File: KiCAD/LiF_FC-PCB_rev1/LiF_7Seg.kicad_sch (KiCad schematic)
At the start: 9 parts, among them J33 DISP 5V0_{EN}, U13 74HCT595PW,118, U14 DC56-11EWA, U15 74HCT595PW,118

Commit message: fixing ERC bugs on schematic. Only MCU left
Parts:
- added TP29: DATA, TestPoint:TestPoint_Bridge_Pitch2.54mm_Drill1.0mm, symbol Connector:TestPoint
- added TP30: CLK, TestPoint:TestPoint_Bridge_Pitch2.54mm_Drill1.0mm, symbol Connector:TestPoint
- added TP31: LATCH, TestPoint:TestPoint_Bridge_Pitch2.54mm_Drill1.0mm, symbol Connector:TestPoint
- added TP32: GND, TestPoint:TestPoint_Bridge_Pitch2.54mm_Drill1.0mm, symbol Connector:TestPoint
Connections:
- net GND: now also TP32.1
- net SSEG.CLK: now also TP30.1
- net SSEG.DATA: now also TP29.1
- net SSEG.LATCH: now also TP31.1

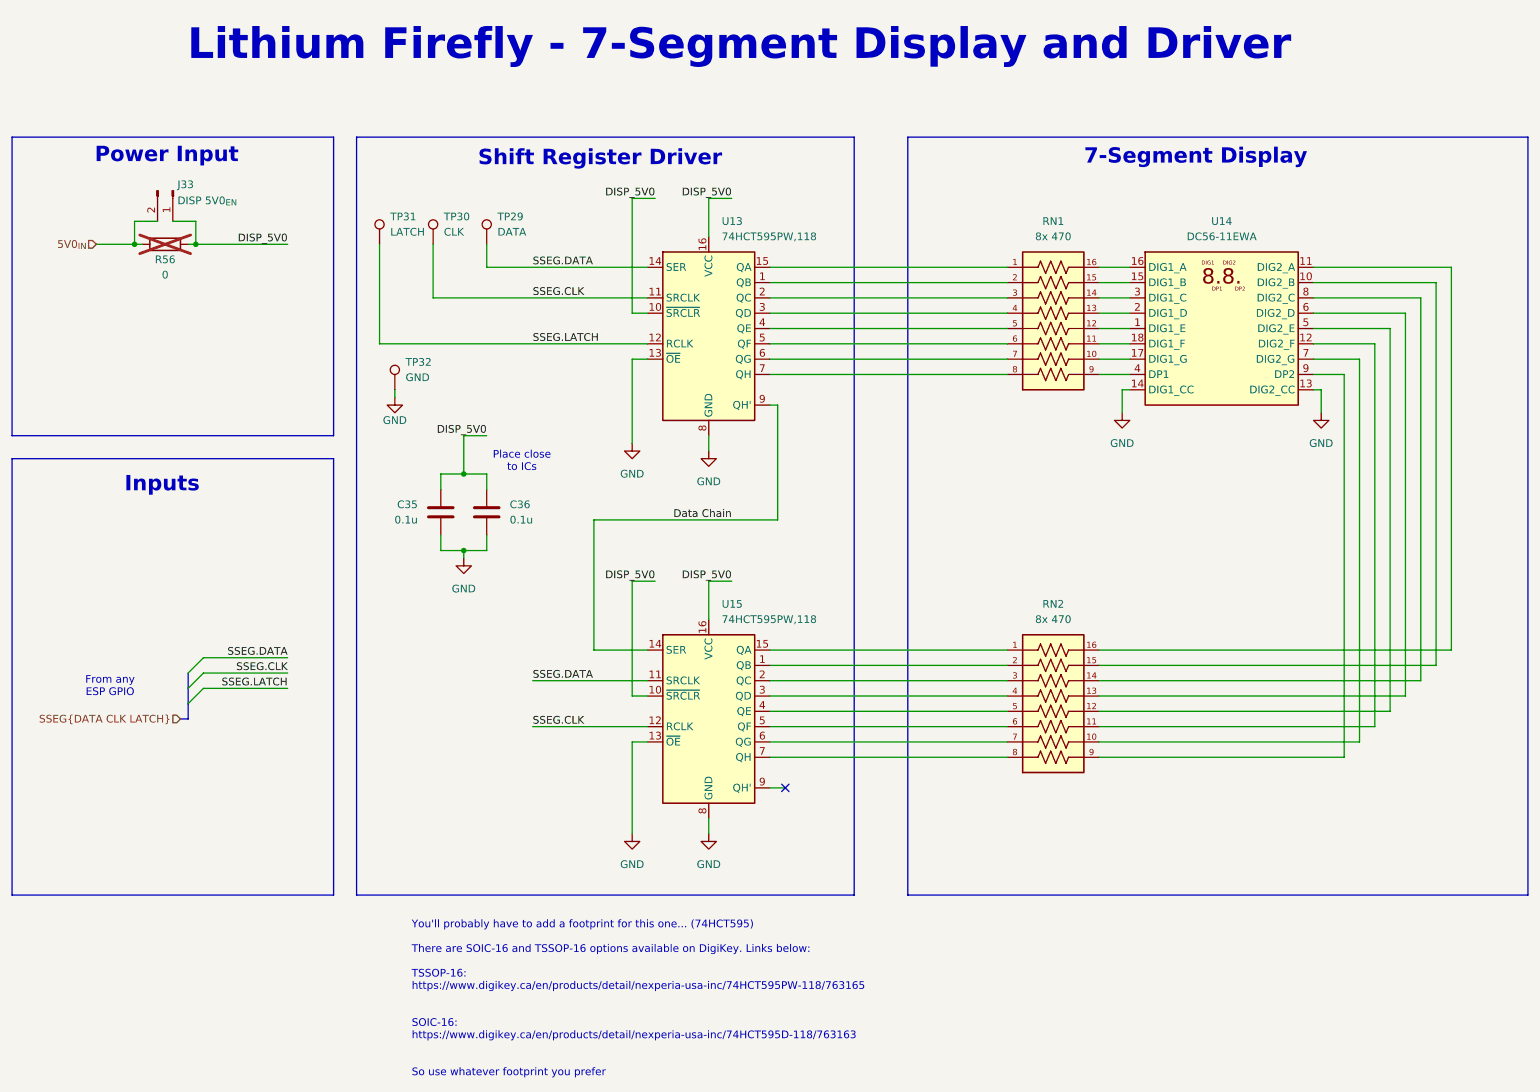
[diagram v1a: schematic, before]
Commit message: Added MCU pinout, shanged shift registers to GPIO expanders to save pins on MCU
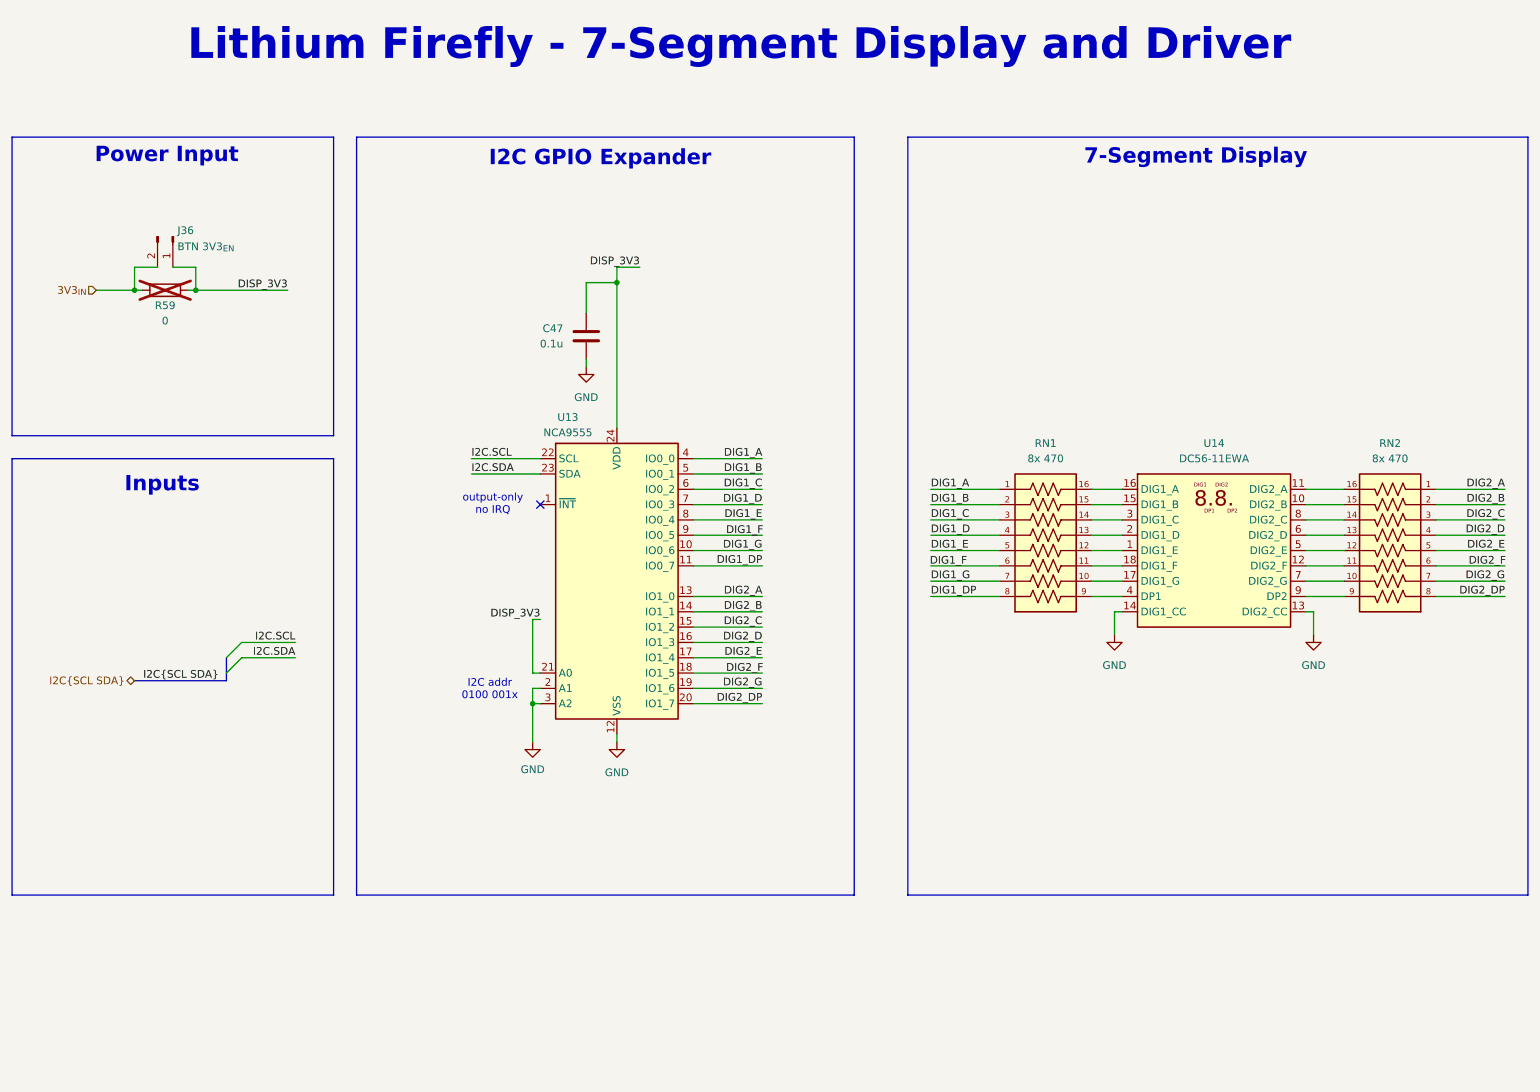
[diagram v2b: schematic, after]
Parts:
- removed C35, C36: 0.1u, Capacitor_SMD:C_0805_2012Metric, symbol Device:C
- removed J33: DISP 5V0_{EN}, Connector_PinHeader_2.54mm:PinHeader_1x02_P2.54mm_Vertical, symbol Connector:Conn_01x02_Pin
- removed R56: 0, Resistor_SMD:R_0805_2012Metric, symbol Device:R
- removed TP29: DATA, TestPoint:TestPoint_Bridge_Pitch2.54mm_Drill1.0mm, symbol Connector:TestPoint
- removed TP30: CLK, TestPoint:TestPoint_Bridge_Pitch2.54mm_Drill1.0mm, symbol Connector:TestPoint
- removed TP31: LATCH, TestPoint:TestPoint_Bridge_Pitch2.54mm_Drill1.0mm, symbol Connector:TestPoint
- removed TP32: GND, TestPoint:TestPoint_Bridge_Pitch2.54mm_Drill1.0mm, symbol Connector:TestPoint
- removed U13, U15: 74HCT595PW,118, Package_SO:TSSOP-16_4.4x5mm_P0.65mm, symbol 74xx:74HCT595
- added C47: 0.1u, Capacitor_SMD:C_0805_2012Metric, symbol Device:C
- added J36: BTN 3V3_{EN}, Connector_PinHeader_2.54mm:PinHeader_1x02_P2.54mm_Vertical, symbol Connector:Conn_01x02_Pin
- added R59: 0, Resistor_SMD:R_0805_2012Metric, symbol Device:R
- added U13: NCA9555, Package_SO:TSSOP-24_4.4x7.8mm_P0.65mm, symbol Interface_Expansion:PCA9555PW
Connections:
- net GND: now also C47.2, U13.12 (VSS), U13.2 (A1), U13.3 (A2)
- net DIG1_B: now reaches RN1.2
- net DIG1_B: now also U13.5 (IO0_1)
- net DIG1_A: now reaches RN1.1
- net DIG1_A: now also U13.4 (IO0_0)
- net DIG1_C: now reaches RN1.3
- net DIG1_C: now also U13.6 (IO0_2)
- net DIG1_D: now reaches RN1.4
- net DIG1_D: now also U13.7 (IO0_3)
- net DIG1_E: now reaches RN1.5
- net DIG1_E: now also U13.8 (IO0_4)
- net DIG1_G: now reaches RN1.7
- net DIG1_G: now also U13.10 (IO0_6)
- net DIG1_DP: now reaches RN1.8
- net DIG1_DP: now also U13.11 (IO0_7)
- net DIG2_A: now reaches RN2.1
- net DIG2_A: now also U13.13 (IO1_0)
- net DIG2_B: now reaches RN2.2
- net DIG2_B: now also U13.14 (IO1_1)
- net DIG2_C: now reaches RN2.3
- net DIG2_C: now also U13.15 (IO1_2)
- net DIG2_D: now reaches RN2.4
- net DIG2_D: now also U13.16 (IO1_3)
- net DIG2_E: now reaches RN2.5
- net DIG2_E: now also U13.17 (IO1_4)
- net DIG2_G: now reaches RN2.7
- net DIG2_G: now also U13.19 (IO1_6)
- net DIG2_DP: now reaches RN2.8
- net DIG2_DP: now also U13.20 (IO1_7)
- new net 3V3_{IN}: J36.2 (Pin_2), R59.2
- new net DISP_3V3: C47.1, J36.1 (Pin_1), R59.1, U13.21 (A0), U13.24 (VDD)
- new net I2C.SCL: U13.22 (SCL)
- new net I2C.SDA: U13.23 (SDA)
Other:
- note added: "I2C GPIO Expander"
- note added: "I2C addr 0100 001x"
- note added: "output-only no IRQ"
- note removed: "From any ESP GPIO"
- note removed: "Place close to ICs"
- note removed: "Shift Register Driver"
- note removed: "You'll probably have to add a footprint for this one... (74HCT595) There are SOIC-16 and TSSOP-16 options available on DigiKey. Links below: TSSOP-16: https://www.digikey.ca/en/products/detail/nexperia-usa-inc/74HCT595PW-118/763165 SOIC-16: https://www.digikey.ca/en/products/detail/nexperia-usa-inc/74HCT595D-118/763163 So use whatever footprint you prefer"
- title: (none) -> Lithium Firefly Custom FC/CC PCB
- moved on the sheet: RN1, RN2, U14

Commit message: Finalized schematic diagram. Only needs formatting fixes and resistor component sourcing info
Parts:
- renumbered C47 to C42, J36 to J37, R59 to R60, U14 to U13, U13 to U14
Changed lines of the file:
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@@
 		(dnp no)
 		(fields_autoplaced yes)
-		(property "Reference" "#PWR081"
+		(property "Reference" "#PWR084"
 			(at 236.22 123.19 0)
 			(effects
@@
 			(project "LiF_FC-PCB_rev1"
 				(path "/9e3e8da7-e506-46c9-90e5-307e4ad30d29/d823ad92-d1a3-4f4d-8dfc-d728d5836dc0"
-					(reference "#PWR081")
+					(reference "#PWR084")
 					(unit 1)
 				)
@@
 		(on_board yes)
 		(dnp no)
-		(property "Reference" "J36"
+		(property "Reference" "J37"
 			(at 47.752 49.784 90)
 			(effects
@@
 			(project "LiF_FC-PCB_rev1"
 				(path "/9e3e8da7-e506-46c9-90e5-307e4ad30d29/d823ad92-d1a3-4f4d-8dfc-d728d5836dc0"
-					(reference "J36")
+					(reference "J37")
 					(unit 1)
 				)
@@
 		(dnp no)
 		(fields_autoplaced yes)
-		(property "Reference" "U14"
+		(property "Reference" "U13"
 			(at 219.71 85.09 0)
 			(effects
@@
 			(project "LiF_FC-PCB_rev1"
 				(path "/9e3e8da7-e506-46c9-90e5-307e4ad30d29/d823ad92-d1a3-4f4d-8dfc-d728d5836dc0"
-					(reference "U14")
+					(reference "U13")
 					(unit 1)
 				)
@@
 		(dnp no)
 		(fields_autoplaced yes)
-		(property "Reference" "#PWR085"
+		(property "Reference" "#PWR086"
 			(at 120.65 140.97 0)
 			(effects
@@
 			(project "LiF_FC-PCB_rev1"
 				(path "/9e3e8da7-e506-46c9-90e5-307e4ad30d29/d823ad92-d1a3-4f4d-8dfc-d728d5836dc0"
-					(reference "#PWR085")
+					(reference "#PWR086")
 					(unit 1)
 				)
@@
 		(on_board yes)
 		(dnp no)
-		(property "Reference" "U13"
+		(property "Reference" "U14"
 			(at 112.522 80.772 0)
 			(effects
@@
 			(project "LiF_FC-PCB_rev1"
 				(path "/9e3e8da7-e506-46c9-90e5-307e4ad30d29/d823ad92-d1a3-4f4d-8dfc-d728d5836dc0"
-					(reference "U13")
+					(reference "U14")
 					(unit 1)
 				)
@@
 		(on_board yes)
 		(dnp no)
-		(property "Reference" "C47"
+		(property "Reference" "C42"
 			(at 111.76 66.0399 0)
 			(effects
@@
 			(project "LiF_FC-PCB_rev1"
 				(path "/9e3e8da7-e506-46c9-90e5-307e4ad30d29/d823ad92-d1a3-4f4d-8dfc-d728d5836dc0"
-					(reference "C47")
+					(reference "C42")
 					(unit 1)
 				)
@@
 		(dnp no)
 		(fields_autoplaced yes)
-		(property "Reference" "#PWR080"
+		(property "Reference" "#PWR083"
 			(at 203.2 123.19 0)
 			(effects
@@
 			(project "LiF_FC-PCB_rev1"
 				(path "/9e3e8da7-e506-46c9-90e5-307e4ad30d29/d823ad92-d1a3-4f4d-8dfc-d728d5836dc0"
-					(reference "#PWR080")
+					(reference "#PWR083")
 					(unit 1)
 				)
@@
 		(on_board yes)
 		(dnp no)
-		(property "Reference" "#PWR083"
+		(property "Reference" "#PWR085"
 			(at 106.68 140.97 0)
 			(effects
@@
 			(project "LiF_FC-PCB_rev1"
 				(path "/9e3e8da7-e506-46c9-90e5-307e4ad30d29/d823ad92-d1a3-4f4d-8dfc-d728d5836dc0"
-					(reference "#PWR083")
+					(reference "#PWR085")
 					(unit 1)
 				)
@@
 		(on_board yes)
 		(dnp yes)
-		(property "Reference" "R59"
+		(property "Reference" "R60"
 			(at 45.72 62.23 90)
 			(effects
@@
 			(project "LiF_FC-PCB_rev1"
 				(path "/9e3e8da7-e506-46c9-90e5-307e4ad30d29/d823ad92-d1a3-4f4d-8dfc-d728d5836dc0"
-					(reference "R59")
+					(reference "R60")
 					(unit 1)
 				)

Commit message: backup before expanding the board size
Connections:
- net DIG1_A: now also RN1.8; no longer RN1.1
- net DIG1_B: now also RN1.7; no longer RN1.2
- net DIG1_C: now also RN1.6; no longer RN1.3
- net DIG1_D: now also RN1.5; no longer RN1.4
- net DIG1_DP: now also RN1.1; no longer RN1.8
- net DIG1_E: now also RN1.4; no longer RN1.5
- net DIG1_F: now also RN1.3, U14.9 (IO0_5)
- net DIG1_G: now also RN1.2; no longer RN1.7
- net DIG2_A: now also RN2.8; no longer RN2.1
- net DIG2_B: now also RN2.7; no longer RN2.2
- net DIG2_C: now also RN2.6; no longer RN2.3
- net DIG2_D: now also RN2.5; no longer RN2.4
- net DIG2_DP: now also RN2.1; no longer RN2.8
- net DIG2_E: now also RN2.4; no longer RN2.5
- net DIG2_F: now also RN2.3, U14.18 (IO1_5)
- net DIG2_G: now also RN2.2; no longer RN2.7
- net at U13.1 (DIG1_E): now also RN1.13; no longer RN1.12
- net at U13.10 (DIG2_B): now also RN2.10; no longer RN2.15
- net at U13.11 (DIG2_A): now also RN2.9; no longer RN2.16
- net at U13.12 (DIG2_F): now also RN2.14; no longer RN2.11
- net at U13.15 (DIG1_B): now also RN1.10; no longer RN1.15
- net at U13.16 (DIG1_A): now also RN1.9; no longer RN1.16
- net at U13.17 (DIG1_G): now also RN1.15; no longer RN1.10
- net at U13.18 (DIG1_F): now also RN1.14; no longer RN1.11
- net at U13.2 (DIG1_D): now also RN1.12; no longer RN1.13
- net at U13.3 (DIG1_C): now also RN1.11; no longer RN1.14
- net at U13.4 (DP1): now also RN1.16; no longer RN1.9
- net at U13.5 (DIG2_E): now also RN2.13; no longer RN2.12
- net at U13.6 (DIG2_D): now also RN2.12; no longer RN2.13
- net at U13.7 (DIG2_G): now also RN2.15; no longer RN2.10
- net at U13.8 (DIG2_C): now also RN2.11; no longer RN2.14
- net at U13.9 (DP2): now also RN2.16; no longer RN2.9
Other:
- moved on the sheet: RN2
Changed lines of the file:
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@@
 	)
 	(label "DIG2_F"
-		(at 268.1351 105.5316 180)
+		(at 267.97 105.41 180)
 		(effects
 			(font
@@
 	)
 	(label "DIG1_F"
-		(at 172.5549 105.5316 0)
+		(at 172.72 105.41 0)
 		(effects
 			(font
@@
 	)
 	(label "DIG2_F"
-		(at 144.9451 123.3116 180)
+		(at 144.78 123.19 180)
 		(effects
 			(font
@@
 	)
 	(label "DIG1_F"
-		(at 144.9451 100.4516 180)
+		(at 144.78 100.33 180)
 		(effects
 			(font
@@
 	(symbol
 		(lib_id "LiF_PCB_Symbols:EXB-2HV471JV")
-		(at 191.77 100.33 0)
+		(at 191.77 102.87 0)
+		(mirror x)
 		(unit 1)
 		(exclude_from_sim no)
@@
 		(on_board yes)
 		(dnp no)
-		(fields_autoplaced yes)
 		(property "Reference" "RN1"
-			(at 191.77 85.09 0)
+			(at 191.77 118.11 0)
 			(effects
 				(font
@@
 		)
 		(property "Value" "8x 470"
-			(at 191.77 87.63 0)
+			(at 191.77 115.57 0)
 			(effects
 				(font
@@
 		)
 		(property "Footprint" "LiF_PCB_Footprints:RESCAXE50P380X160X55-16N"
-			(at 188.976 84.836 0)
+			(at 188.976 118.364 0)
 			(effects
 				(font
@@
 		)
 		(property "Datasheet" "https://industrial.panasonic.com/cdbs/www-data/pdf/AOC0000/AOC0000C14.pdf"
-			(at 191.77 100.33 0)
+			(at 191.77 102.87 0)
 			(effects
 				(font
@@
 		)
 		(property "Description" "RES ARRAY 8 RES 470 OHM 1506"
-			(at 191.77 100.33 0)
+			(at 191.77 102.87 0)
 			(effects
 				(font
@@
 		)
 		(property "PN" "EXB-2HV471JV"
-			(at 191.77 100.33 0)
+			(at 191.77 102.87 0)
 			(effects
 				(font
@@
 		)
 		(property "DKPN" "Y1471CT-ND"
-			(at 191.77 100.33 0)
+			(at 191.77 102.87 0)
 			(effects
 				(font
@@
 		)
 		(property "DigiKey_Part_Number" ""
-			(at 191.77 100.33 0)
+			(at 191.77 102.87 0)
 			(effects
 				(font
@@
 		)
 		(property "SnapEDA_Link" "https://www.snapeda.com/parts/EXB-2HV471JV/Panasonic/view-part/?ref=snap"
-			(at 188.976 84.836 0)
+			(at 188.976 118.364 0)
 			(effects
 				(font
@@
 		)
 		(property "MAXIMUM_PACKAGE_HEIGHT" "0.55mm"
-			(at 191.77 100.33 0)
+			(at 191.77 102.87 0)
 			(effects
 				(font
@@
 		)
 		(property "CREATOR" "ASHISH"
-			(at 191.77 100.33 0)
+			(at 191.77 102.87 0)
 			(effects
 				(font
@@
 		)
 		(property "Package" "1506 Panasonic"
-			(at 191.77 100.33 0)
+			(at 191.77 102.87 0)
 			(effects
 				(font
@@
 		)
 		(property "Check_prices" "https://www.snapeda.com/parts/EXB-2HV471JV/Panasonic/view-part/?ref=eda"
-			(at 188.976 84.836 0)
+			(at 188.976 118.364 0)
 			(effects
 				(font
@@
 		)
 		(property "STANDARD" "IPC-7351B"
-			(at 191.77 100.33 0)
+			(at 191.77 102.87 0)
 			(effects
 				(font
@@
 		)
 		(property "PARTREV" "1-Mar-20"
-			(at 191.77 100.33 0)
+			(at 191.77 102.87 0)
 			(effects
 				(font
@@
 		)
 		(property "VERIFIER" ""
-			(at 191.77 100.33 0)
+			(at 191.77 102.87 0)
 			(effects
 				(font
@@
 		)
 		(property "MF" "Panasonic Electronic"
-			(at 191.77 100.33 0)
+			(at 191.77 102.87 0)
 			(effects
 				(font
@@
 		)
 		(property "MP" "EXB-2HV471JV"
-			(at 191.77 100.33 0)
+			(at 191.77 102.87 0)
 			(effects
 				(font
@@
 		)
 		(property "Description_1" "470 Ohm ±5% 62.5mW Power Per Element Isolated 8 Resistor Network/Array ±200ppm/°C 1506, Convex, Long Side Terminals"
-			(at 188.976 84.836 0)
+			(at 188.976 118.364 0)
 			(effects
 				(font
@@
 		)
 		(property "MANUFACTURER" "Panasonic"
-			(at 191.77 100.33 0)
+			(at 191.77 102.87 0)
 			(effects
 				(font
@@
 	(symbol
 		(lib_id "LiF_PCB_Symbols:EXB-2HV471JV")
-		(at 248.92 100.33 0)
-		(mirror y)
+		(at 248.92 102.87 180)
 		(unit 1)
 		(exclude_from_sim no)
@@
 		(on_board yes)
 		(dnp no)
-		(fields_autoplaced yes)
 		(property "Reference" "RN2"
-			(at 248.92 85.09 0)
+			(at 248.92 118.11 0)
 			(effects
 				(font
@@
 		)
 		(property "Value" "8x 470"
-			(at 248.92 87.63 0)
+			(at 248.92 115.57 0)
 			(effects
 				(font
@@
 		)
 		(property "Footprint" "LiF_PCB_Footprints:RESCAXE50P380X160X55-16N"
-			(at 251.714 84.836 0)
+			(at 251.714 118.364 0)
 			(effects
 				(font
@@
 		)
 		(property "Datasheet" "https://industrial.panasonic.com/cdbs/www-data/pdf/AOC0000/AOC0000C14.pdf"
-			(at 248.92 100.33 0)
+			(at 248.92 102.87 0)
 			(effects
 				(font
@@
 		)
 		(property "Description" "RES ARRAY 8 RES 470 OHM 1506"
-			(at 248.92 100.33 0)
+			(at 248.92 102.87 0)
 			(effects
 				(font
@@
 		)
 		(property "PN" "EXB-2HV471JV"
-			(at 248.92 100.33 0)
+			(at 248.92 102.87 0)
 			(effects
 				(font
@@
 		)
 		(property "DKPN" "Y1471CT-ND"
-			(at 248.92 100.33 0)
+			(at 248.92 102.87 0)
 			(effects
 				(font
@@
 		)
 		(property "DigiKey_Part_Number" ""
-			(at 248.92 100.33 0)
+			(at 248.92 102.87 0)
 			(effects
 				(font
@@
 		)
 		(property "SnapEDA_Link" "https://www.snapeda.com/parts/EXB-2HV471JV/Panasonic/view-part/?ref=snap"
-			(at 251.714 84.836 0)
+			(at 251.714 118.364 0)
 			(effects
 				(font
@@
 		)
 		(property "MAXIMUM_PACKAGE_HEIGHT" "0.55mm"
-			(at 248.92 100.33 0)
+			(at 248.92 102.87 0)
 			(effects
 				(font
@@
 		)
 		(property "CREATOR" "ASHISH"
-			(at 248.92 100.33 0)
+			(at 248.92 102.87 0)
 			(effects
 				(font
@@
 		)
 		(property "Package" "1506 Panasonic"
-			(at 248.92 100.33 0)
+			(at 248.92 102.87 0)
 			(effects
 				(font
@@
 		)
 		(property "Check_prices" "https://www.snapeda.com/parts/EXB-2HV471JV/Panasonic/view-part/?ref=eda"
-			(at 251.714 84.836 0)
+			(at 251.714 118.364 0)
 			(effects
 				(font
@@
 		)
 		(property "STANDARD" "IPC-7351B"
-			(at 248.92 100.33 0)
+			(at 248.92 102.87 0)
 			(effects
 				(font
@@
 		)
 		(property "PARTREV" "1-Mar-20"
-			(at 248.92 100.33 0)
+			(at 248.92 102.87 0)
 			(effects
 				(font
@@
 		)
 		(property "VERIFIER" ""
-			(at 248.92 100.33 0)
+			(at 248.92 102.87 0)
 			(effects
 				(font
@@
 		)
 		(property "MF" "Panasonic Electronic"
-			(at 248.92 100.33 0)
+			(at 248.92 102.87 0)
 			(effects
 				(font
@@
 		)
 		(property "MP" "EXB-2HV471JV"
-			(at 248.92 100.33 0)
+			(at 248.92 102.87 0)
 			(effects
 				(font
@@
 		)
 		(property "Description_1" "470 Ohm ±5% 62.5mW Power Per Element Isolated 8 Resistor Network/Array ±200ppm/°C 1506, Convex, Long Side Terminals"
-			(at 251.714 84.836 0)
+			(at 251.714 118.364 0)
 			(effects
 				(font
@@
 		)
 		(property "MANUFACTURER" "Panasonic"
-			(at 248.92 100.33 0)
-			(effects
-				(font
+			(at 248.92 102.87 0)
+			(effects
+				(font

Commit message: backup before leaving school
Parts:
- J37: footprint Connector_PinHeader_2.54mm:PinHeader_1x02_P2.54mm_Vertical -> Connector_PinHeader_2.54mm:PinHeader_1x02_P2.54mm_Vertical_SMD_Pin1Left
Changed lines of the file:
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@@
 			)
 		)
-		(property "Footprint" "Connector_PinHeader_2.54mm:PinHeader_1x02_P2.54mm_Vertical"
+		(property "Footprint" "Connector_PinHeader_2.54mm:PinHeader_1x02_P2.54mm_Vertical_SMD_Pin1Left"
 			(at 46.99 50.8 0)
 			(effects
